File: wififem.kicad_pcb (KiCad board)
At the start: 2 copper layers, 40 x 49.5 mm, 46 parts, among them J1 Conn_Coaxial, J2 Conn_Coaxial, J3 Conn_Coaxial, J4 Conn_01x05, U1 MCP6566, U2 74HCT04, U3 SE2611T, U4 AP1117-15

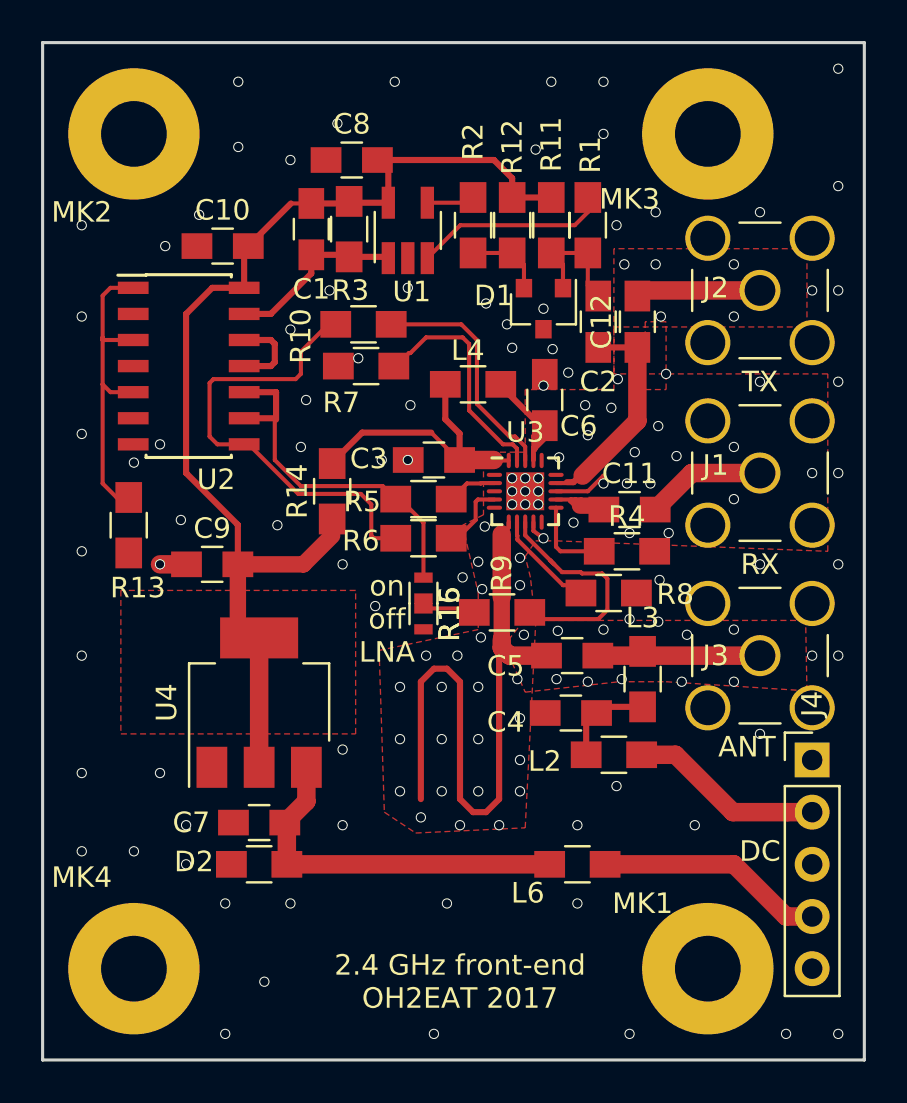
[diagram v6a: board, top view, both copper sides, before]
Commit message: Add 2.2u decoupling, some layout changes
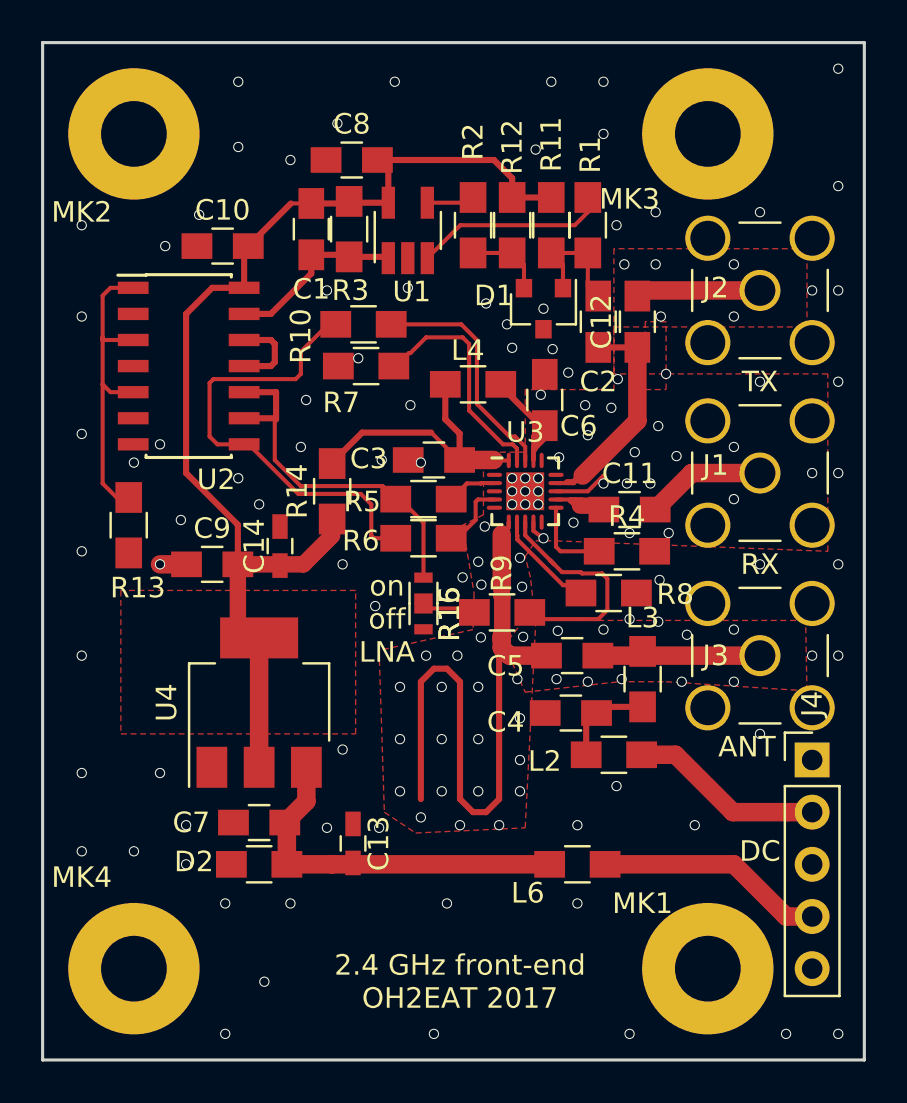
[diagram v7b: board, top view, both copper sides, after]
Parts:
- added C13: 2u2, Capacitors_SMD:C_0603_HandSoldering, F.Cu at (101.5, 82.5)
- added C14: 2u2, Capacitors_SMD:C_0603_HandSoldering, F.Cu at (97.9, 68.1)
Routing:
- net +3V3: track 56.0 -> 58.1 mm
- net Net-(C13-Pad2): track 18.0 -> 19.0 mm
- net GND: vias 146 -> 147

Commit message: Some final changes
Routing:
- net GND: vias 147 -> 173
